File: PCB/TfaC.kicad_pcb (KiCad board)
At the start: 2 copper layers, 105 x 54 mm, 59 parts, among them IC501 ATMEGA88-A, M301 DisplayModule, P101 Line, P501 PRG, Q401 IRLML2502, Q402 IRLML2502, Q403 IRLML2502, Q404 IRLML2502, Q405 IRLML2502, Q406 IRLML2502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

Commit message: Shifted the ISP to a more sensible location
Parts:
- moved P501 22.2 mm to (193.5, 89.0), turned to 0 degrees
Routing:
- net Sleep: track 44.9 -> 83.9 mm
- net /Controller/MISO: track 94.4 -> 120.5 mm
- net /Controller/MOSI: track 107.5 -> 128.5 mm, vias 1 -> 2
- net /Controller/SCK: track 125.5 -> 134.9 mm
- net /Controller/Vcc: track 110.2 -> 105.2 mm
- net /Controller/~DISPLAY_SELECT: track 29.4 -> 25.4 mm
- net /Controller/Reset: track 89.1 -> 85.9 mm, vias 1 -> 2
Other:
- board text added: "MOSI ~SS~ SCK Vcc GND Rst"
- board text removed: "MISO ~SS~ SCK Vcc GND Rst"

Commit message: Cleaned up some more routes
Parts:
- moved SW507 8.98 mm to (165.2, 94.7)
- moved D501 5.21 mm to (172.6, 104.4)
- moved R502 4.95 mm to (170.3, 103.9)
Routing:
- net Sleep: track 83.9 -> 75.9 mm
- net /Controller/SCK: track 134.9 -> 142.7 mm, vias 2 -> 1
- net /Controller/MOSI: track 128.5 -> 135.4 mm
- net /Controller/MISO: track 120.5 -> 113.8 mm, vias 1 -> 2
- net /Controller/Heartbeat: track 9.25 -> 14.5 mm
- net Auto_Time: track 18.6 -> 21.4 mm
- net /Controller/~RTC_SELECT: track 115.7 -> 118.4 mm
- net Summer_Time: track 16.6 -> 14.8 mm

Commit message: Added alarm
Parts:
- R502: moved to B.Cu
- moved D501 19.7 mm to (161.9, 87.9)
- moved R502 18.1 mm to (161.9, 87.9)
- moved SW505 4.85 mm to (159.3, 103.4)
- moved SW507 2.90 mm to (162.7, 96.1)
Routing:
- net /Controller/Heartbeat: track 14.5 -> 18.4 mm, vias 0 -> 2
- net Summer_Time: track 14.8 -> 17.5 mm
- net Auto_Time: track 21.4 -> 23.7 mm
- net GND: track 38.7 -> 40.4 mm, vias 5 -> 6
- net Net-(D501-Pad1): track 2.37 -> 3.47 mm, vias 0 -> 1
- net Alarm_Set: track 19.8 -> 18.7 mm
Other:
- board text added: "K"
- board text added: "MOSI ~SS~ SCK +5 GND Rst"
- board text removed: "MOSI ~SS~ SCK Vcc GND Rst"

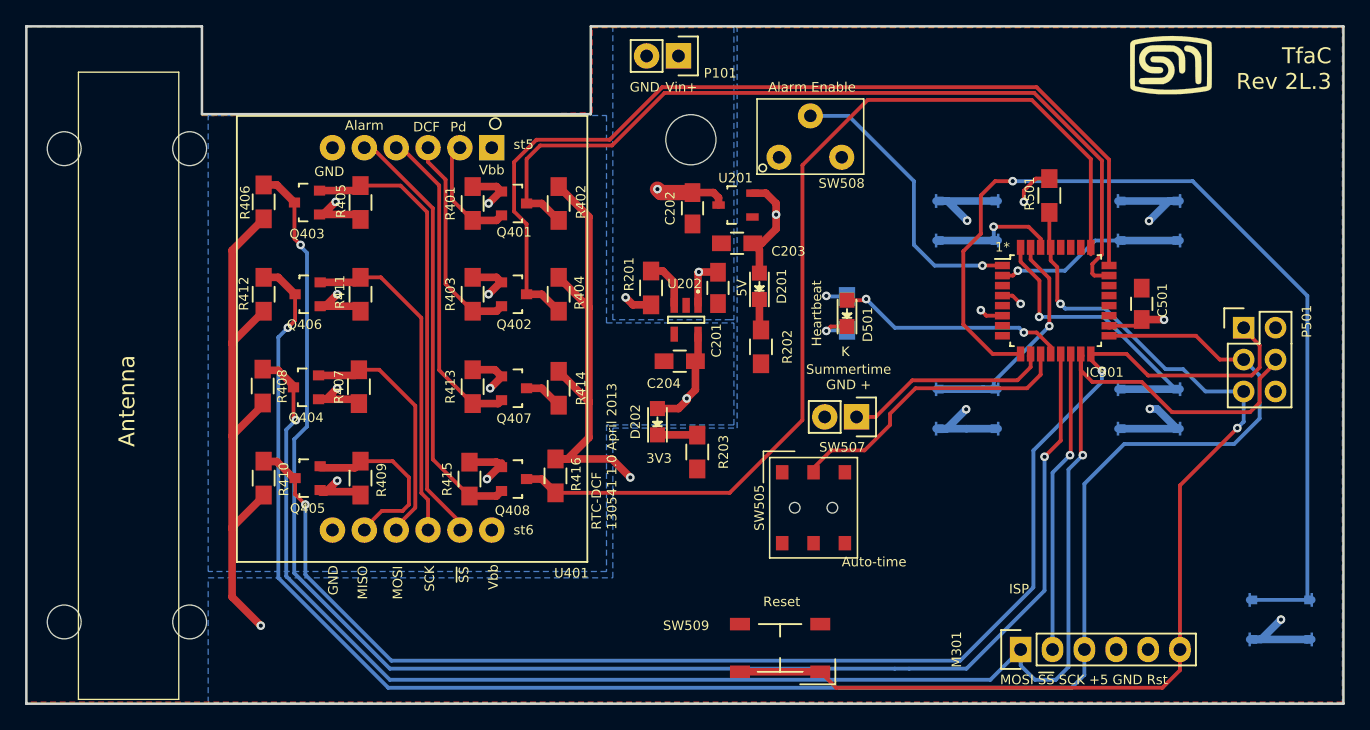
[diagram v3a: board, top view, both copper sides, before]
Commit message: Re-organised the board to incorporate the MISO
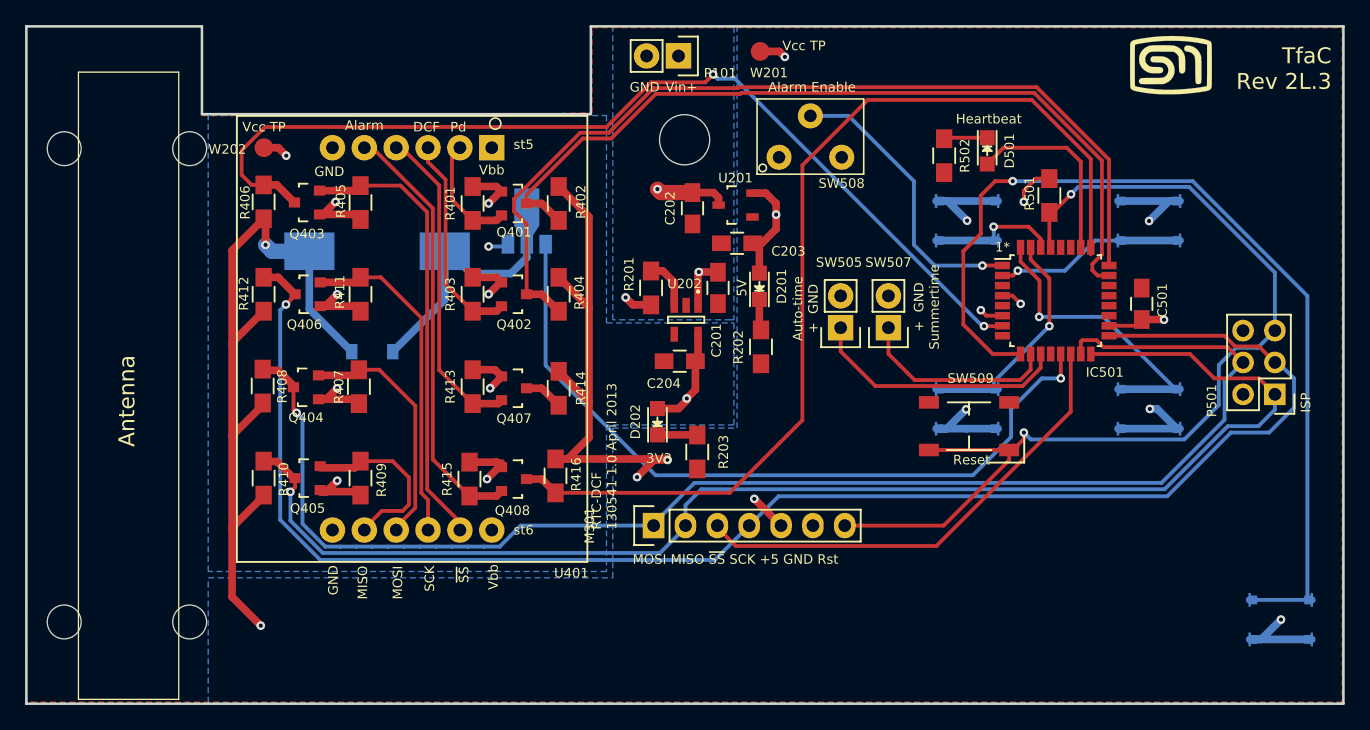
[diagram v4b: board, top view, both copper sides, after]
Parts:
- added D503: 1N4148W, Diodes_SMD:SOD-123, B.Cu at (124.1, 90.9)
- added Q501: 2SD2391, TO_SOT_Packages_SMD:SOT89-3_Housing, B.Cu at (136.4, 80.5)
- added SP501: CT-1205-SMT, tfac-footprints:CT-1205-SMT, B.Cu at (124.5, 82.9)
- added W201: TEST_1P, Measurement_Points:Measurement_Point_Round-SMD-Pad_Small, F.Cu at (155.0, 67.0)
- added W202: TEST_1P, Measurement_Points:Measurement_Point_Round-SMD-Pad_Small, F.Cu at (115.4, 74.7)
- M301: footprint Pin_Headers:Pin_Header_Straight_1x06 -> Pin_Headers:Pin_Header_Straight_1x07
- R502: moved to F.Cu
- SW505: value Auto Time -> AUTO_TIME; footprint tfac-footprints:AYZ0202AGRLC -> Pin_Headers:Pin_Header_Straight_1x02
- moved M301 30.9 mm to (146.5, 104.8)
- moved SW509 23.2 mm to (171.7, 96.9)
- moved D501 17.1 mm to (173.1, 74.9), turned to 270 degrees
- moved R502 14.8 mm to (169.7, 75.3), turned to 90 degrees
- moved SW505 14.5 mm to (161.4, 89.0), turned to 180 degrees
- moved SW507 7.55 mm to (165.2, 89.0), turned to 180 degrees
- moved P501 5.86 mm to (196.0, 94.3), turned to 180 degrees
- moved MNT1 0.50 mm to (149.0, 74.0)
- renumbered REF** to MNT1
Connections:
- IC501 pad 12: /Controller/Heartbeat -> Net-(IC501-Pad12)
- IC501 pad 13: /Controller/~RTC_SELECT -> /Controller/Buzzer
- IC501 pad 26: Net-(IC501-Pad26) -> /Controller/Heartbeat
- IC501 pad 7: Net-(IC501-Pad7) -> /Controller/~RTC_SELECT
- M301 pad 2: /Controller/~DISPLAY_SELECT -> /Controller/MISO
- M301 pad 3: /Controller/SCK -> /Controller/~DISPLAY_SELECT
- M301 pad 4: /Controller/Vcc -> /Controller/SCK
- M301 pad 5: GND -> /Controller/Vcc
- M301 pad 6: /Controller/Reset -> GND
- SW505 pad 1: Net-(SW505-Pad1) -> Auto_Time
- SW505 pad 2: Auto_Time -> GND
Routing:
- net /Controller/Buzzer: track 0.00 -> 61.3 mm, vias 0 -> 1
- net /Controller/~RTC_SELECT: track 118.4 -> 78.6 mm
- net /Controller/Vcc: track 105.2 -> 129.8 mm, vias 7 -> 11
- net Net-(D503-Pad2): track 0.00 -> 23.2 mm
- net /Controller/MOSI: track 135.4 -> 112.9 mm, vias 2 -> 1
- net /Controller/SCK: track 142.7 -> 127.4 mm
- net /Controller/~DISPLAY_SELECT: track 25.4 -> 38.0 mm, vias 1 -> 0
- net /Controller/Reset: track 85.9 -> 79.5 mm
- net /Controller/MISO: track 113.8 -> 109.9 mm, vias 2 -> 1
- net /Controller/Heartbeat: track 18.4 -> 15.3 mm, vias 2 -> 0
- net Auto_Time: track 23.7 -> 20.7 mm
- net /Power System/Vbb: track 46.6 -> 48.6 mm, vias 9 -> 10
- net /Controller/Periodic_INT: track 67.7 -> 65.8 mm
- net /Controller/DCF_RCPT: track 74.8 -> 73.1 mm
- net Summer_Time: track 17.5 -> 15.9 mm
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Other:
- board text added: "+ GND Summertime"
- board text added: "Auto-time + GND"
- board text added: "MOSI MISO ~SS~ SCK +5 GND Rst"
- board text added: "Vcc TP"
- board text removed: "Auto-time"
- board text removed: "K"
- board text removed: "MOSI ~SS~ SCK +5 GND Rst"
- board text removed: "Summertime GND +"

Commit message: Revision 2L_3 Gerbers and sent to OSHPark
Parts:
- moved W202 33.0 mm to (143.5, 92.1)
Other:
- board text added: "Vbb TP"
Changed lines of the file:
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@@
     (links 165)
     (no_connects 0)
-    (area 96.399999 64.899999 201.600001 119.100001)
+    (area 93.941899 63.8107 202.222101 119.100001)
     (thickness 1.6)
     (drawings 69)
@@
   )
   (setup
-    (last_trace_width 0.6096)
+    (last_trace_width 0.1524)
     (user_trace_width 0.3048)
     (user_trace_width 0.6096)
@@
     (tags SOT-23)
     (attr smd)
-    (fp_text reference Q403 (at -2.5 0 360) (layer F.SilkS)
+    (fp_text reference Q403 (at -2.3876 0 360) (layer F.SilkS)
       (effects (font (size 0.762 0.762) (thickness 0.127)))
     )
@@
     (tags SOT-23A)
     (attr smd)
-    (fp_text reference U201 (at 2.159 0 360) (layer F.SilkS)
+    (fp_text reference U201 (at 0 3.0226 90) (layer F.SilkS)
       (effects (font (size 0.762 0.762) (thickness 0.127)))
     )
@@
     (tags "Mesurement Point Round SMD Pad 1.5mm")
     (attr virtual)
-    (fp_text reference W201 (at 0.702 1.707) (layer F.SilkS)
+    (fp_text reference W201 (at 0.702 1.707) (layer F.SilkS) hide
       (effects (font (size 0.762 0.762) (thickness 0.127)))
     )
@@
   )
   (module Measurement_Points:Measurement_Point_Round-SMD-Pad_Small (layer F.Cu)
-    (at 115.443 74.676)
+    (at 143.4592 92.1004)
     (descr "Mesurement Point, Round, SMD Pad, DM 1.5mm,")
     (tags "Mesurement Point Round SMD Pad 1.5mm")
     (attr virtual)
-    (fp_text reference W202 (at -2.921 0.127) (layer F.SilkS)
+    (fp_text reference W202 (at 2.5654 -0.508) (layer F.SilkS) hide
       (effects (font (size 0.762 0.762) (thickness 0.127)))
     )
@@
     (descr "Through hole pin header")
     (tags "pin header")
-    (fp_text reference M301 (at 0 -5.1 90) (layer F.SilkS)
+    (fp_text reference M301 (at 2.4384 -0.254 180) (layer F.SilkS)
       (effects (font (size 0.762 0.762) (thickness 0.127)))
     )
@@
   (gr_line (start 124.46 80.518) (end 124.46 70.866) (angle 90) (layer Eco1.User) (width 0.0762))
   (gr_line (start 202.184 80.518) (end 93.98 80.518) (angle 90) (layer Eco1.User) (width 0.0762))
-  (gr_text "Vcc TP" (at 115.443 73.025) (layer F.SilkS)
+  (gr_text "Vbb TP" (at 143.9164 90.3732) (layer F.SilkS)
     (effects (font (size 0.762 0.762) (thickness 0.127)))
   )
@@
     (effects (font (size 0.762 0.762) (thickness 0.127)) (justify mirror))
   )
-  (gr_text "RTC-DCF\n130541 1.0 April 2013" (at 142.5702 105.1306 90) (layer F.SilkS)
+  (gr_text "RTC-DCF\n130541 1.0 April 2013" (at 142.6464 107.7976 90) (layer F.SilkS)
     (effects (font (size 0.762 0.762) (thickness 0.127)) (justify left))
   )
@@
   (segment (start 169.375 97.075) (end 171.45 97.075) (width 0.6096) (layer B.Cu) (net 2) (status 10))
   (segment (start 171.45 97.075) (end 173.625 97.075) (width 0.6096) (layer B.Cu) (net 2) (status 20))
-  (segment (start 115.443 74.676) (end 116.586 74.676) (width 0.6096) (layer F.Cu) (net 3))
-  (via (at 117.221 75.311) (size 0.6858) (drill 0.3302) (layers F.Cu B.Cu) (net 3))
-  (segment (start 116.586 74.676) (end 117.221 75.311) (width 0.6096) (layer F.Cu) (net 3))
+  (segment (start 143.4592 92.1004) (end 143.4592 93.3196) (width 0.3048) (layer F.Cu) (net 3))
+  (via (at 144.272 94.1324) (size 0.6858) (drill 0.3302) (layers F.Cu B.Cu) (net 3))
+  (segment (start 143.4592 93.3196) (end 144.272 94.1324) (width 0.3048) (layer F.Cu) (net 3))
   (segment (start 149.1488 94.6658) (end 149.1488 94.8182) (width 0.6096) (layer F.Cu) (net 3))
   (segment (start 148.49602 95.47098) (end 146.812 95.47098) (width 0.6096) (layer F.Cu) (net 3) (status 20))
@@
   (segment (start 146.558 99.568) (end 145.1864 100.9396) (width 0.6096) (layer F.Cu) (net 30))
   (via (at 145.1864 100.9396) (size 0.6858) (drill 0.3302) (layers F.Cu B.Cu) (net 30))
-  (segment (start 156.6672 104.8004) (end 154.5336 102.6668) (width 0.6096) (layer F.Cu) (net 30) (status 400000))
+  (segment (start 156.6672 104.8004) (end 154.5336 102.6668) (width 0.6096) (layer F.Cu) (net 30))
   (via (at 154.5336 102.6668) (size 0.6858) (drill 0.3302) (layers F.Cu B.Cu) (net 30))
-  (segment (start 138.684 99.488) (end 147.5448 99.488) (width 0.6096) (layer F.Cu) (net 30) (status 400000))
+  (segment (start 138.684 99.488) (end 147.5448 99.488) (width 0.6096) (layer F.Cu) (net 30))
   (segment (start 147.5448 99.488) (end 147.6248 99.568) (width 0.6096) (layer F.Cu) (net 30))
   (via (at 147.6248 99.568) (size 0.6858) (drill 0.3302) (layers F.Cu B.Cu) (net 30))
@@
   (segment (start 178.054 82.51) (end 178.162 82.618) (width 0.3048) (layer F.Cu) (net 35) (status 30))
   (segment (start 178.134 82.59) (end 178.162 82.618) (width 0.1524) (layer F.Cu) (net 35) (status 30))
-  (segment (start 137.89914 82.36966) (end 137.89914 92.02674) (width 0.3048) (layer B.Cu) (net 44) (status 400000))
+  (segment (start 137.89914 82.36966) (end 137.89914 92.02674) (width 0.3048) (layer B.Cu) (net 44))
   (segment (start 137.89914 92.02674) (end 146.6596 100.7872) (width 0.3048) (layer B.Cu) (net 44))
   (segment (start 146.6596 100.7872) (end 171.958 100.7872) (width 0.3048) (layer B.Cu) (net 44))
@@
   (via (at 178.9684 93.0656) (size 0.6858) (drill 0.3302) (layers F.Cu B.Cu) (net 44))
   (segment (start 178.9684 93.0656) (end 178.962 93.0592) (width 0.3048) (layer F.Cu) (net 44))
-  (segment (start 178.962 93.0592) (end 178.962 91.118) (width 0.3048) (layer F.Cu) (net 44) (status 800000))
+  (segment (start 178.962 93.0592) (end 178.962 91.118) (width 0.3048) (layer F.Cu) (net 44))
   (segment (start 178.9684 91.1244) (end 178.962 91.118) (width 0.3048) (layer F.Cu) (net 44))
   (segment (start 179.0192 91.1752) (end 178.962 91.118) (width 0.3048) (layer F.Cu) (net 44))
